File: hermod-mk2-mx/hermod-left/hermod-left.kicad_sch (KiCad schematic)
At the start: 45 parts, among them J1 USB_C_Receptacle_USB2.0, J2 Conn_01x05, J3 USB_C_Receptacle_USB2.0, Q3 MMUN2133LT1G, U1 STM32G474CETx, U2 PRTR5V0U2X, U3 XC6206PxxxMR-Regulator_Linear, U4 CR2013-MI2120, U5 PRTR5V0U2X, U8 SN74AHCT1G125DBVR

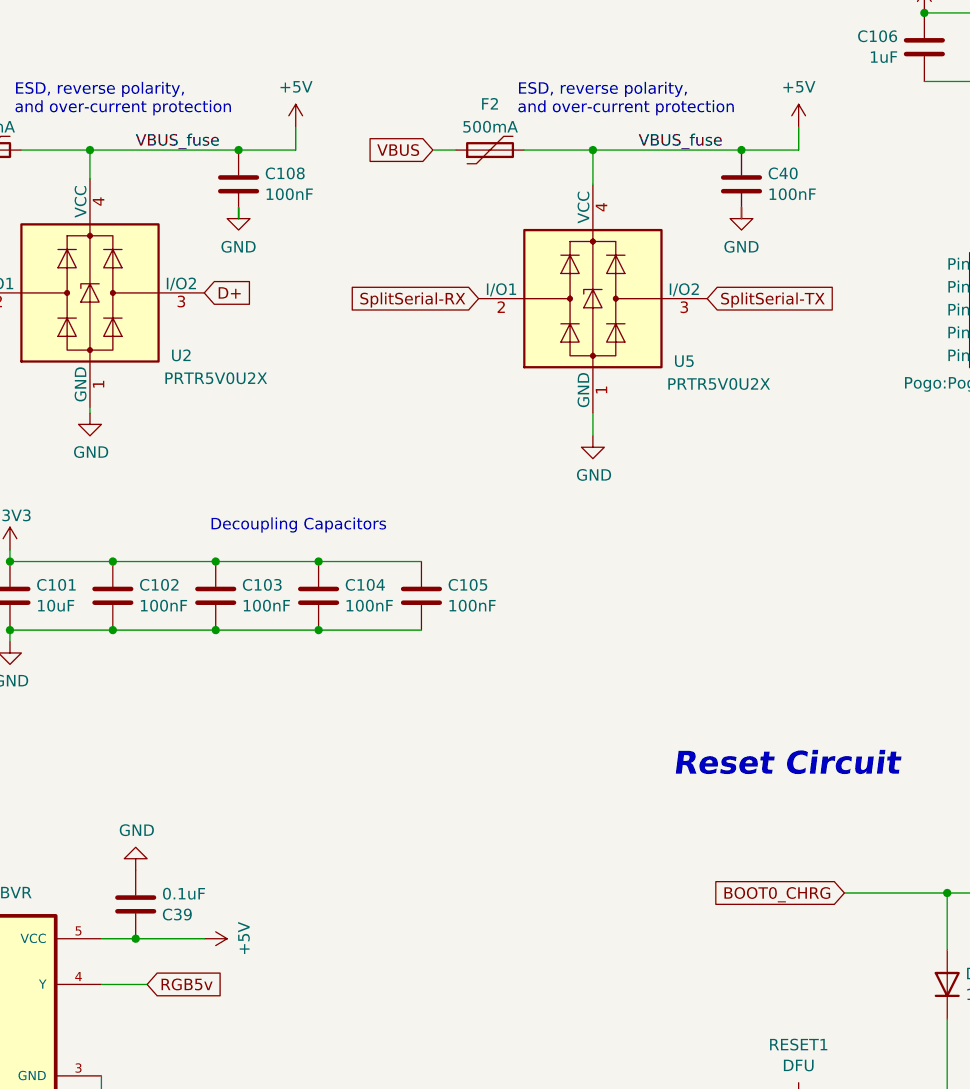
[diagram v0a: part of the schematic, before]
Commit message: Added switches to hermod 3 and updated mist thumb spacing
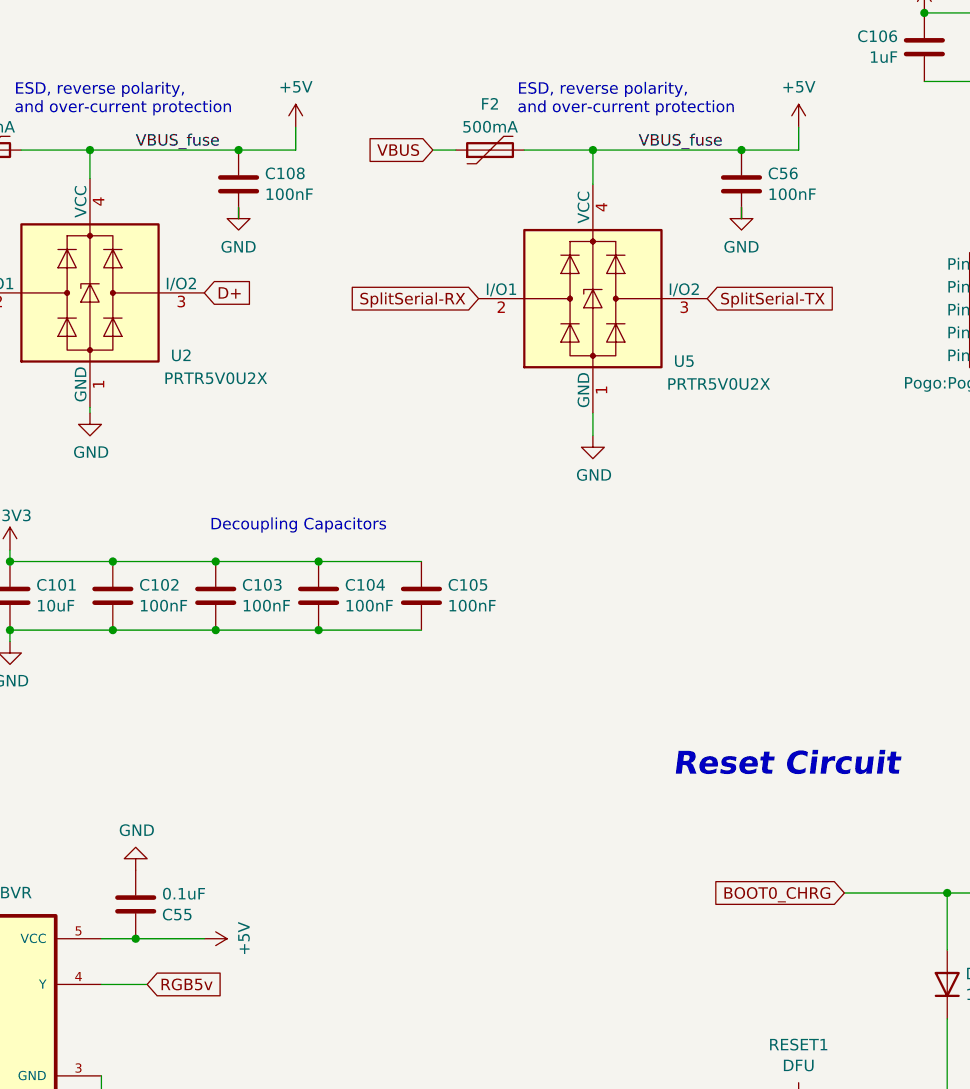
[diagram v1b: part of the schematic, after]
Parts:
- renumbered C39 to C55, C40 to C56
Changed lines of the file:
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@@
 		(on_board yes)
 		(dnp no)
-		(property "Reference" "C40"
+		(property "Reference" "C56"
 			(at 179.451 138.5316 0)
 			(effects
@@
 			(project "hermod-left"
 				(path "/cb32b2da-a60d-4ed4-a57b-2c397f553171"
-					(reference "C40")
+					(reference "C56")
 					(unit 1)
 				)
@@
 		(on_board yes)
 		(dnp no)
-		(property "Reference" "C39"
+		(property "Reference" "C55"
 			(at 112.141 220.8784 0)
 			(effects
@@
 			(project "hermod-left"
 				(path "/cb32b2da-a60d-4ed4-a57b-2c397f553171"
-					(reference "C39")
-					(unit 1)
-				)
+					(reference "C55")
+					(unit 1)
+				)
